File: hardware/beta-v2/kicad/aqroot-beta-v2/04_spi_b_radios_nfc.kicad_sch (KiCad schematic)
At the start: 44 parts, among them J7 BM02B-ACHSS-GAN-ETF, U7 E07-400M10S, U8 E22-900M22S, U9 ST25R3916-AQET, Y1 27.12MHz 10pF 3225-4P

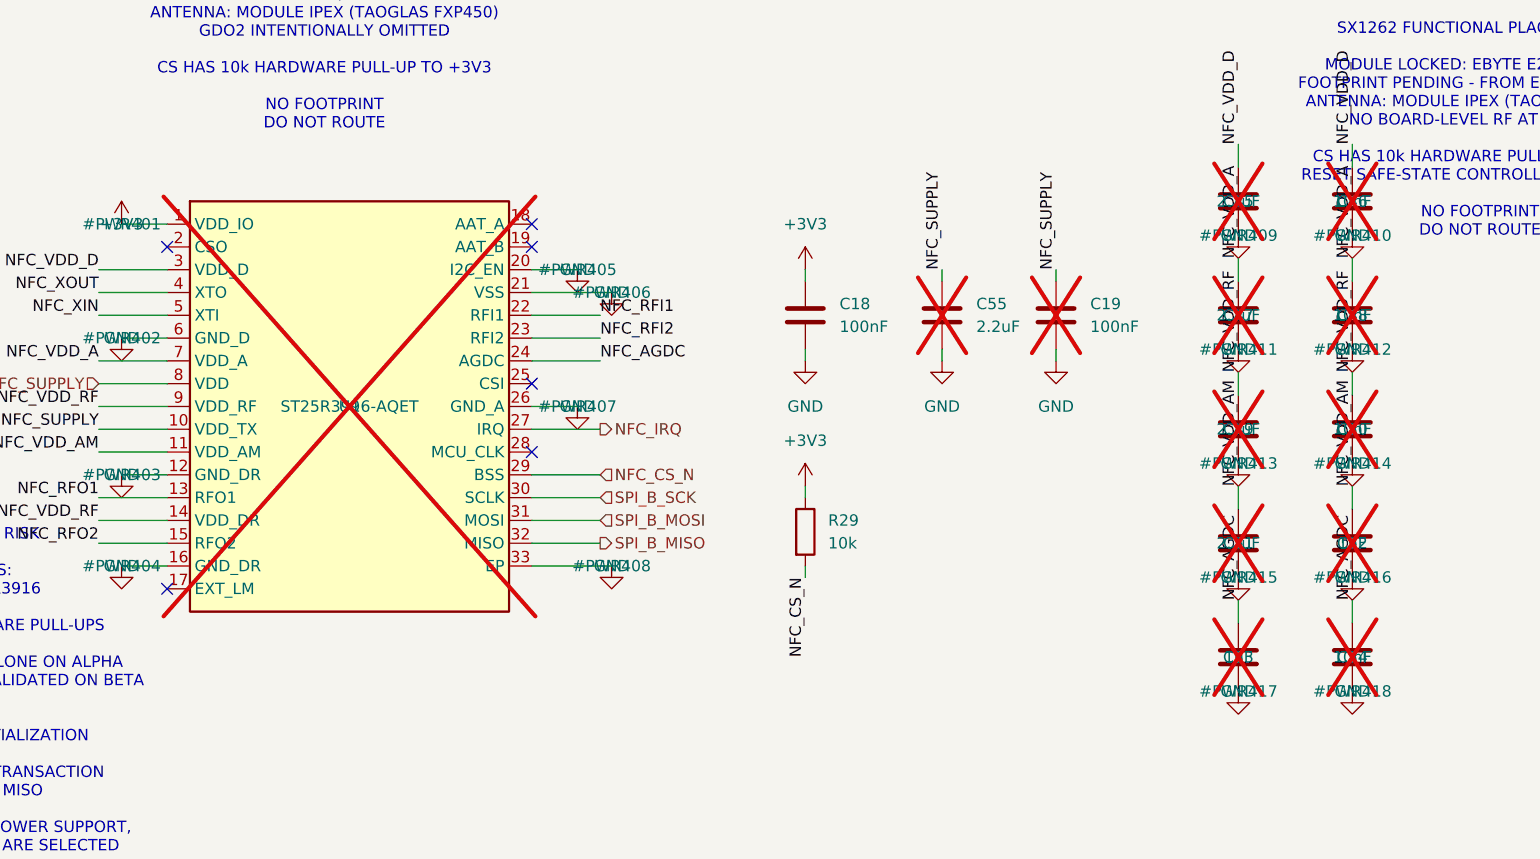
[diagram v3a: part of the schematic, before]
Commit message: hardware: close Full Beta v2 pre-placement schematic issues
FBV2-S2-001 pre-placement release audit. The audit found a fabrication-blocking
defect on the first thing it looked at.

U9 ST25R3916-AQET and its twelve mandatory supply-decoupling capacitors (C19,
C45-C55) were still marked DNP, inherited from Beta-DM, against D-035 ("NFC is
mandatory in the FIRST Full Beta v2 fabrication. No DNP showcase shortcut") and
D-055 ("NFC must be FITTED and functional on the first fabrication"). Everything
around the chip was already fitted - the 27.12 MHz crystal, the complete
differential matching network, the antenna connector, the SPI wiring. The first
five boards would have carried a finished 13.56 MHz front end with no NFC chip
on it. All thirteen parts are now FIT. Seventh consecutive sheet with a
load-bearing inherited DNP.

Six missing MPNs added: D9 -> PMEG2010AEH,115 and Q4/Q6-Q9 -> BSS138LT1G. Every
active and every connector now carries an exact MPN.

Two undocumented placeholders resolved. R68 is a 0R DNP bypass across SW9, the
hard power switch - fitting it wires the unit permanently ON and defeats the
only way to power down a hung or unflashed board; it is now marked DNP AND IT
MUST STAY DNP. C21/C22 are dead pads with one terminal no-connect flagged.

Two stale "FOOTPRINT STILL BLOCKED" notes on L1 and L2 withdrawn - both land
patterns had already been built from the manufacturer drawings. L1 and L4
headroom recorded: 1.4x and 2.8x on Isat, which closes B-68.

16 DNP parts remain and every one is documented. Zero unexplained DNP.

ERC 27 / 0 errors / 27, unchanged. 0 duplicate references, 0 unresolved
footprint references, 0 orphan nets, 0 *_TBD. fork_equivalence.py PASS,
netclass_probe.py PASS. PCB untouched and still bit-identical to Beta-DM. No
PCB placement or routing was started.

Co-Authored-By: Claude Opus 5 <noreply@anthropic.com>
Claude-Session: https://claude.ai/code/session_0133CdFHfKcCH8oPWqJZWe7o
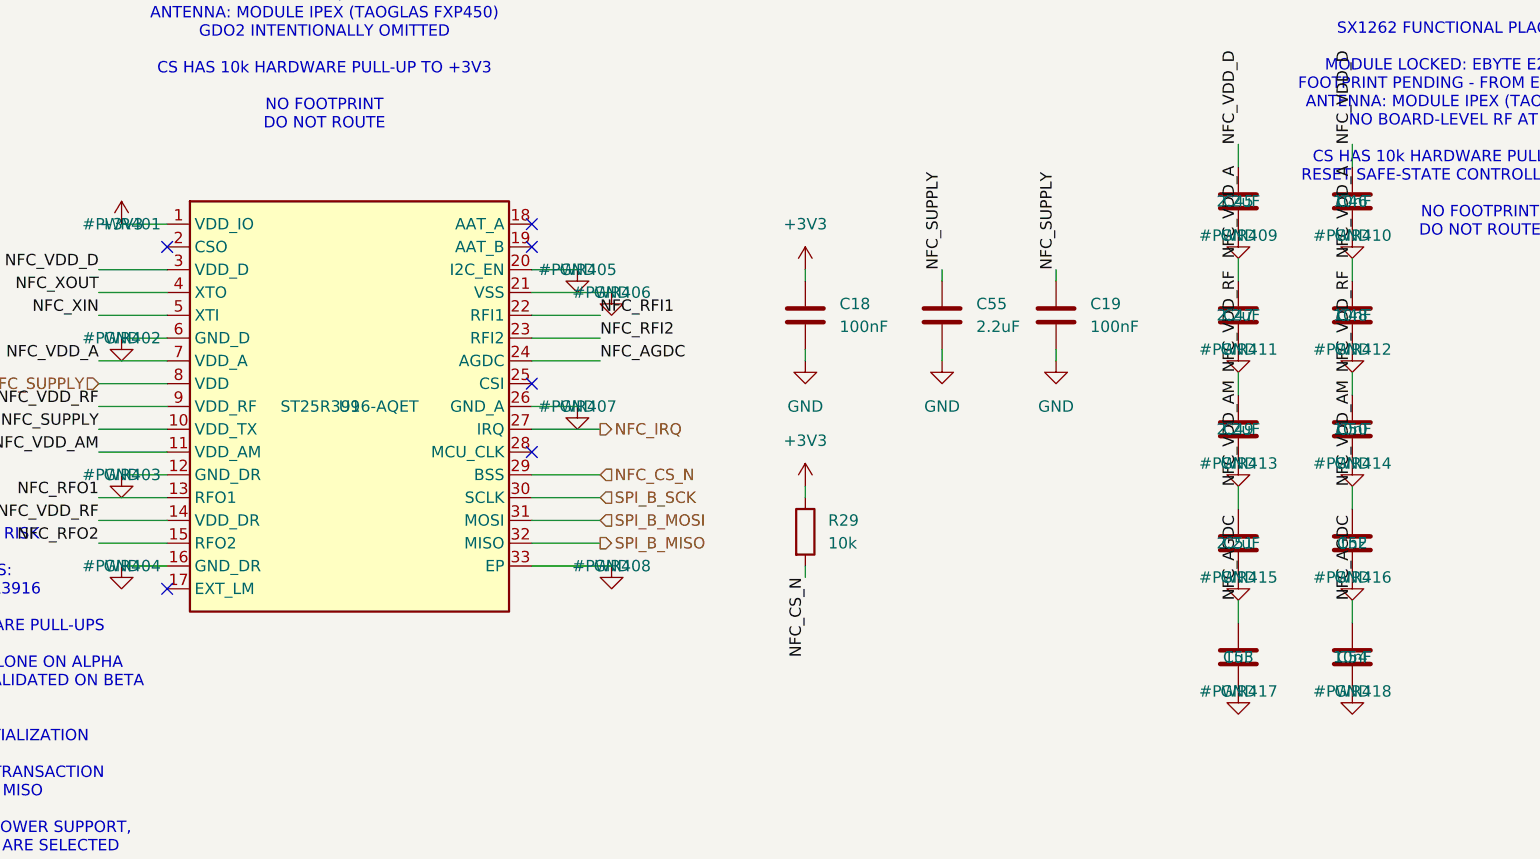
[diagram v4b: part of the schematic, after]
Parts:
- C19: Note ST25R3916 external VDD / VDD_TX high-frequency decoupling: 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 -> FBV2-S2-001: **DNP -> FIT**. ST25R3916 supply decoupling, m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; now fitted
- C45, C46, C47, C48, C49, C50, C51, C52, C53, C54: Note (none) -> FBV2-S2-001: **DNP -> FIT**. ST25R3916 supply decoupling, m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; now fitted
- C55: Note ST25R3916 VDD / VDD_TX local BULK decoupling for pulsed NFC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 -> FBV2-S2-001: **DNP -> FIT**. ST25R3916 supply decoupling, m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; now fitted
- U9: Note (none) -> FBV2-S2-001: **DNP -> FIT**. `U9` AND ITS ENTIRE SUPPLY-DEC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; now fitted

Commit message: hardware: close Full Beta v2 S2 release blockers
Closes B-03, B-63, B-70 and B-71's schematic-side work. Property-only
changes to the nine sheets plus the microphone footprint; ERC unchanged
at 27 / 0 errors / 27 with an identical violation histogram, and the PCB
is untouched and still bit-identical to Beta-DM.

B-03 - all eight remaining Tier-2 footprints compared dimension by
dimension against retrieved manufacturer drawings. Y1 moves from
candidate to lock (Yajingxin TXM27.12M0004322DBBDO00T, C362365, 3421 in
stock) with a land that matches the vendor's Suggested Layout exactly.
The MAX98357A looked like a genuine defect - outline 21-0136 gives
T1633-5 an EP of 1.50/1.60/1.70 while the land is 1.23 - and is not:
land pattern 90-0032 Rev E is issued for T1633-5, -5C and -7C together
and specifies one land for all three, so no project-local footprint was
created.

B-63 - the microphone acoustic port is now drawn rather than described.
1.05 mm NPTH taken from the drawing's own pad-4 ring inner diameter,
paste pulled back 0.10 mm as a declared stencil choice, keepout marked,
bottom-port orientation recorded.

B-70 - L5/L6 lock to Murata LQW18AN39NG80D. The DCR is a first-order
term here: 0.20 ohm max against R_q = 1.1 ohm drops network Q from 25.3
to about 21.4, so the antenna must be tuned with this exact part fitted
and the first lever is R_q, not 39 nH.

B-71 - 65 LCSC fields written in, three MPN strings corrected. J6 and J7
carried bare order codes that resolve to zero-stock listings while the
plating-suffixed strings are abundantly stocked. Six substitution traps
recorded in the symbols themselves, including BAT54W offered for
BAT54WS - a single diode for a series pair - and a clone for the battery
reverse-polarity pass FETs.

Eight DNP parts still carried no recorded reason and now do. The design
has zero unexplained DNP.

Co-Authored-By: Claude Opus 5 <noreply@anthropic.com>
Claude-Session: https://claude.ai/code/session_0133CdFHfKcCH8oPWqJZWe7o
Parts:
- J7: LCSC (none) -> C5118738; MPN BM02B-ACHSS-GAN-ETF -> BM02B-ACHSS-GAN-ETF(LF)(SN); Note2 (none) -> SOURCING 2026-08-23 (FBV2-S2-002) (B-71). The bare order co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
- L5, L6: LCSC (none) -> C2042966; MPN (none) -> LQW18AN39NG80D; Manufacturer (none) -> Murata Electronics; Note (none) -> B-70 CLOSED 2026-08-23 (FBV2-S2-002). Murata LQW18AN39NG80D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
- U7: LCSC (none) -> C2965513
- U9: Note2 (none) -> SOURCING 2026-08-23 (FBV2-S2-002) (B-71). ST25R3916-AQET is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
- Y1: Note CANDIDATE against a live LCSC listing, not a lock (D-096). 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 -> LOCKED 2026-08-23 (FBV2-S2-002). Yajingxin TXM27.12M0004322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
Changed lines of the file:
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@@
 			)
 		)
+		(property "LCSC" "C2965513"
+			(at 87.63 57.15 0)
+			(hide yes)
+			(show_name no)
+			(do_not_autoplace no)
+			(effects
+				(font
+					(size 1.27 1.27)
+				)
+			)
+		)
 		(property "Manufacturer" "Ebyte (Chengdu Ebyte Electronic Technology)"
 			(at 87.63 57.15 0)
@@
 			)
 		)
+		(property "Note2" "SOURCING 2026-08-23 (FBV2-S2-002) (B-71). ST25R3916-AQET is LCSC C5267441 with STOCK 6 against a need of 5 - one spare, and this is a UFQFPN-32 5x5 with an exposed pad, i.e. the single part on this board that genuinely cannot be hand-placed. Buy spares from a broadline distributor and consign. LCSC/JLC library state verified live on 2026-08-23 through the JLCPCB parts API (D-096). Stock is a snapshot, not a guarantee."
+			(at 91.44 143.51 0)
+			(hide yes)
+			(show_name no)
+			(do_not_autoplace no)
+			(effects
+				(font
+					(size 1.27 1.27)
+				)
+			)
+		)
 		(property "Manufacturer" "STMicroelectronics"
 			(at 91.44 143.51 0)
@@
 			)
 		)
-		(property "Note" "CANDIDATE against a live LCSC listing, not a lock (D-096). 27.12 MHz, 10 pF load, +/-10 ppm, ESR 30 R, -40..+85 C"
+		(property "Note" "LOCKED 2026-08-23 (FBV2-S2-002). Yajingxin TXM27.12M0004322DBBDO00T, LCSC C362365, stock 3421 live on 2026-08-23. Manufacturer data sheet read: SMD3225-4P, 27.120000 MHz fundamental, CL 10 pF, ESR 30 R max, drive level 100 uW max, frequency tolerance +/-10 ppm at 25 C, stability +/-20 ppm over -40..+85 C, aging +/-5 ppm/year, Co 0..5 pF. Total +/-30 ppm is far inside the ISO/IEC 14443 carrier requirement (+/-7 kHz = +/-516 ppm at 13.56 MHz). B-03 FOOTPRINT VERIFIED TIER 1: the data sheet SUGGESTED LAYOUT gives 1.4 x 1.2 mm pads with a 0.8 mm column gap and a 0.5 mm row gap, i.e. centres at (+/-1.10, +/-0.85). Crystal:Crystal_SMD_3225-4Pin_3.2x2.5mm is 1.4 x 1.2 at (+/-1.10, +/-0.85) - EXACT MATCH. Package 3.20 +/-0.1 x 2.50 +/-0.1 x 0.70 +/-0.1; pins 1/3 are the crystal, 2/4 are GND."
 			(at 0 0 0)
 			(hide yes)
@@
 			)
 		)
+		(property "Note" "B-70 CLOSED 2026-08-23 (FBV2-S2-002). Murata LQW18AN39NG80D, 0603/1608 wire-wound ceramic, 39 nH +/-2% (G), Rdc 0.20 R max, SRF 3000 MHz min, Q 37 min, Irated 1 A. CHECKED AGAINST D-134, NOT LOCKED FROM HEADLINE SPECS: (1) SRF 3000 MHz is 74x the 40.68 MHz third harmonic and 149x the 20.1 MHz EMC corner, so the part is a pure inductor across the whole band of interest; (2) X_L = 3.32 R at 13.56 MHz, which is the reactance D-134 already solved the match against; (3) DCR IS NOT NEGLIGIBLE HERE - 0.20 R max sits in series with R_q = 1.1 R, so worst-case arm resistance is 1.30 R and the network Q falls from 25.3 to about 21.4, roughly -15%. That moves FURTHER INTO the safe, under-driven side D-134 deliberately chose, so it is not a stress condition, but the antenna MUST be tuned on the bench with this exact part fitted. If field strength is short at first article the first lever is R_q 1.1 R -> 0.9 R, NOT a change to 39 nH (D-134 forbids moving L without re-running the whole matching calculation); (4) coil current about 187 mA worst case against a 1 A rating, >5x margin. LCSC C2042966, stock 270 on 2026-08-23. LCSC/JLC library state verified live on 2026-08-23 through the JLCPCB parts API (D-096). Stock is a snapshot, not a guarantee."
+			(at 308.61 129.54 0)
+			(hide yes)
+			(show_name no)
+			(do_not_autoplace no)
+			(effects
+				(font
+					(size 1.27 1.27)
+				)
+			)
+		)
+		(property "Manufacturer" "Murata Electronics"
+			(at 308.61 129.54 0)
+			(hide yes)
+			(show_name no)
+			(do_not_autoplace no)
+			(effects
+				(font
+					(size 1.27 1.27)
+				)
+			)
+		)
+		(property "MPN" "LQW18AN39NG80D"
+			(at 308.61 129.54 0)
+			(hide yes)
+			(show_name no)
+			(do_not_autoplace no)
+			(effects
+				(font
+					(size 1.27 1.27)
+				)
+			)
+		)
+		(property "LCSC" "C2042966"
+			(at 308.61 129.54 0)
+			(hide yes)
+			(show_name no)
+			(do_not_autoplace no)
+			(effects
+				(font
+					(size 1.27 1.27)
+				)
+			)
+		)
 		(pin "1"
 		)
@@
 			)
 		)
+		(property "Note" "B-70 CLOSED 2026-08-23 (FBV2-S2-002). Murata LQW18AN39NG80D, 0603/1608 wire-wound ceramic, 39 nH +/-2% (G), Rdc 0.20 R max, SRF 3000 MHz min, Q 37 min, Irated 1 A. CHECKED AGAINST D-134, NOT LOCKED FROM HEADLINE SPECS: (1) SRF 3000 MHz is 74x the 40.68 MHz third harmonic and 149x the 20.1 MHz EMC corner, so the part is a pure inductor across the whole band of interest; (2) X_L = 3.32 R at 13.56 MHz, which is the reactance D-134 already solved the match against; (3) DCR IS NOT NEGLIGIBLE HERE - 0.20 R max sits in series with R_q = 1.1 R, so worst-case arm resistance is 1.30 R and the network Q falls from 25.3 to about 21.4, roughly -15%. That moves FURTHER INTO the safe, under-driven side D-134 deliberately chose, so it is not a stress condition, but the antenna MUST be tuned on the bench with this exact part fitted. If field strength is short at first article the first lever is R_q 1.1 R -> 0.9 R, NOT a change to 39 nH (D-134 forbids moving L without re-running the whole matching calculation); (4) coil current about 187 mA worst case against a 1 A rating, >5x margin. LCSC C2042966, stock 270 on 2026-08-23. LCSC/JLC library state verified live on 2026-08-23 through the JLCPCB parts API (D-096). Stock is a snapshot, not a guarantee."
+			(at 308.61 175.26 0)
+			(hide yes)
+			(show_name no)
+			(do_not_autoplace no)
+			(effects
+				(font
+					(size 1.27 1.27)
+				)
+			)
+		)
+		(property "Manufacturer" "Murata Electronics"
+			(at 308.61 175.26 0)
+			(hide yes)
+			(show_name no)
+			(do_not_autoplace no)
+			(effects
+				(font
+					(size 1.27 1.27)
+				)
+			)
+		)
+		(property "MPN" "LQW18AN39NG80D"
+			(at 308.61 175.26 0)
+			(hide yes)
+			(show_name no)
+			(do_not_autoplace no)
+			(effects
+				(font
+					(size 1.27 1.27)
+				)
+			)
+		)
+		(property "LCSC" "C2042966"
+			(at 308.61 175.26 0)
+			(hide yes)
+			(show_name no)
+			(do_not_autoplace no)
+			(effects
+				(font
+					(size 1.27 1.27)
+				)
+			)
+		)
 		(pin "1"
 		)
@@
 			)
 		)
+		(property "Note2" "SOURCING 2026-08-23 (FBV2-S2-002) (B-71). The bare order code BM02B-ACHSS-GAN-ETF resolves to LCSC C20088622 with STOCK 0; the identical part under JST s lead-free/tin plating suffix, BM02B-ACHSS-GAN-ETF(LF)(SN), is C5118738 with 16260 in stock. The MPN string was corrected to the stocked one. LCSC/JLC library state verified live on 2026-08-23 through the JLCPCB parts API (D-096). Stock is a snapshot, not a guarantee."
+			(at 400.05 129.54 0)
+			(hide yes)
+			(show_name no)
+			(do_not_autoplace no)
+			(effects
+				(font
+					(size 1.27 1.27)
+				)
+			)
+		)
+		(property "LCSC" "C5118738"
+			(at 400.05 129.54 0)
+			(hide yes)
+			(show_name no)
+			(do_not_autoplace no)
+			(effects
+				(font
+					(size 1.27 1.27)
+				)
+			)
+		)
 		(property "Manufacturer" "JST"
 			(at 0 0 0)
@@
 			)
 		)
-		(property "MPN" "BM02B-ACHSS-GAN-ETF"
+		(property "MPN" "BM02B-ACHSS-GAN-ETF(LF)(SN)"
 			(at 0 0 0)
 			(hide yes)
